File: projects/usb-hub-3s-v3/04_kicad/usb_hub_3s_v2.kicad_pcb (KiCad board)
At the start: 4 copper layers, 130 x 92 mm, 114 parts, among them J1 C98732, J2 C503996, J3 C503996, J4 C503996, J5 C5337088, Q1 C2760089, Q2 C404363, Q3 C404363, Q4 C404363, Q5 C404363, Q6 C2760089, Q7 C78284, SW1 C2939728, U10 C7519, U11 C13755, U12 C7519, U2 C13755, U3 C130056, U4 C130056, U5 C130056, U6 C473910, U7 C473910, U8 C7519, U9 C7519

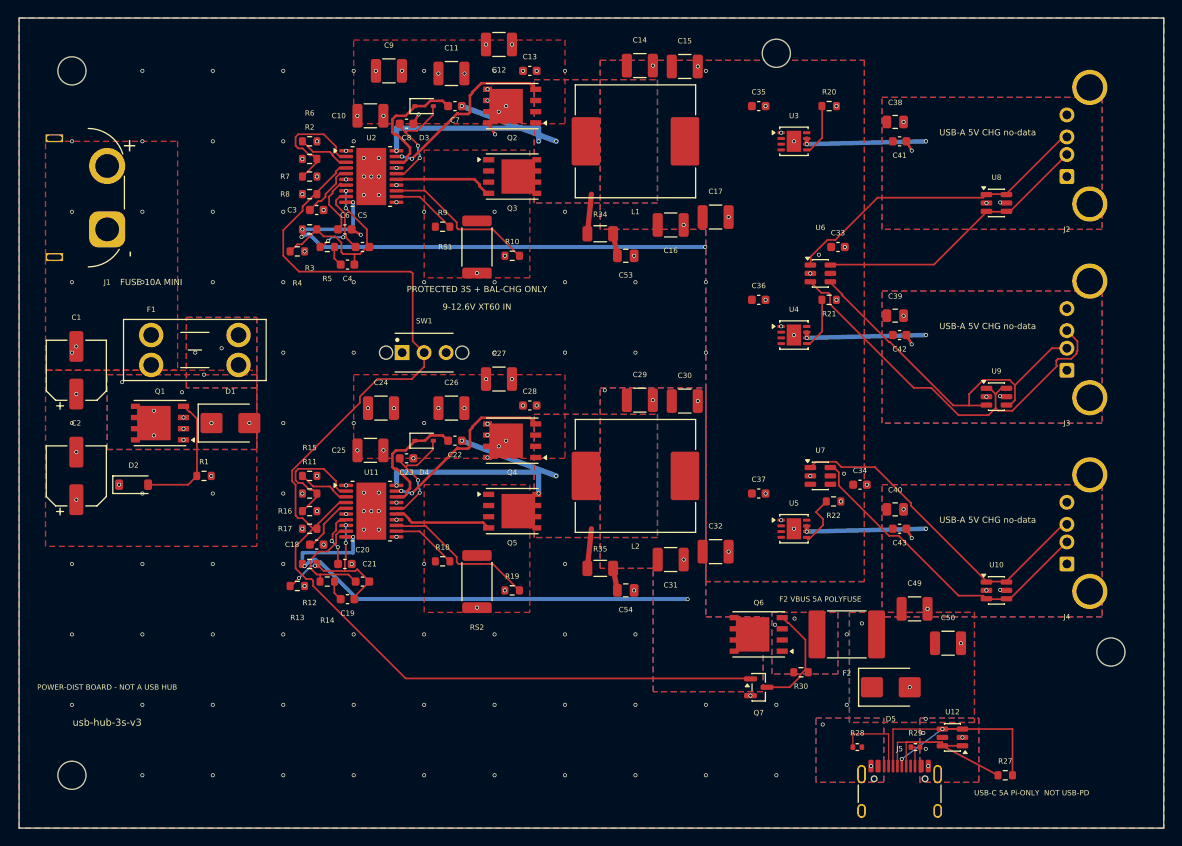
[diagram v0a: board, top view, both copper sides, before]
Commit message: usb-hub-3s-v3 v1.6: DRC 0/0/0 — the H3 screw-short is gone, and 11 CPL rows were off JLC's datum
v1.5 is DO-NOT-ORDER, and not for a reason any render could show. A new A-POS
gate measured every CPL row against JLC's convention — JLC positions a part
from the bounding box of its PAD CENTRES — and found the exporter had been
emitting fp.GetPosition(), the footprint ANCHOR. 11 of 108 rows were off-datum:
J1 4.6861mm, J2/J3/J4 3.7346mm, J5 1.4975mm, Q4/Q5/Q6 0.0625mm. Every external
connector, worst by nearly 5mm.

COPPER, all measured on FILLED zones before and after.

H3 was a short of the 6A rail to GND through a screw. MEASURED on sealed v1.5:
H3 (106,24) is a 1.600mm-radius NPTH whose F.Cu carries GND at 1.850mm AND 5VA
at 1.850mm, and whose B.Cu carries 5VA at 1.850 AND GND at 1.851. 0.250mm of
bare laminate and ~20um of mask, on both faces. EVERY M3 fastener bridges it —
not just a big washer, the smallest cap head (r 2.75) already does. v1.5's only
mitigation was a sentence in ORDER_README about nylon standoffs, which survives
exactly as long as the person who read it.

So v1.6 states a RULE instead of a note: within r <= 4.00mm of any mounting
hole, all outer copper is ONE net and that net is GND. Enforced three ways —
the 5VA pour is notched (5VA now stops at 4.500mm), the router's hole keepout
goes 3.0 -> 4.2mm so a signal wave cannot re-create it on a different net, and
the check is re-measured on the final filled board rather than assumed.

Also: H4's VBUSA3 4.152 -> 5.008mm (a DIN 9021 washer reached it); the In2 VIN
plane 1.850 -> 2.077mm on all four drills (0.250mm to a 12.6V plane, against a
+-0.13mm NPTH position tolerance, buried where no inspection will ever see it).
In1 GND is deliberately left at 1.850 — a grounded fastener touching GND is the
benign case and thinning the return plane costs more than it buys.

VBUS ampacity 0.5 -> 0.8mm. "Pour-fed" was true of the connector end and false
of the feed: each of VBUSA1/2/3 ran 13.554mm of 0.500mm B.Cu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
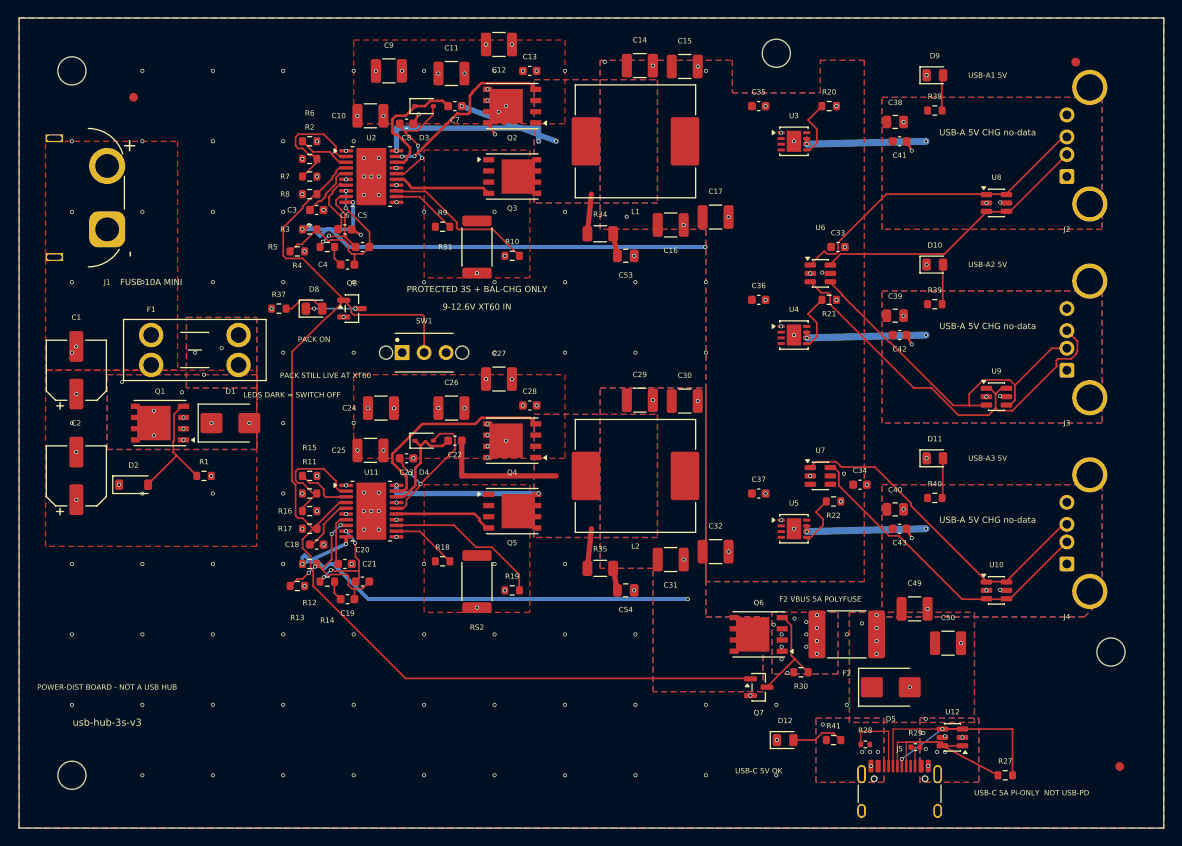
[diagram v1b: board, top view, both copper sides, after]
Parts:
- added D10: C2297, LED_SMD:LED_0805_2012Metric, F.Cu at (124.0, 48.0)
- added D11: C2297, LED_SMD:LED_0805_2012Metric, F.Cu at (124.0, 70.0)
- added D12: C2297, LED_SMD:LED_0805_2012Metric, F.Cu at (107.0, 102.0)
- added D8: C2296, LED_SMD:LED_0805_2012Metric, F.Cu at (53.5, 53.0)
- added D9: C2297, LED_SMD:LED_0805_2012Metric, F.Cu at (124.0, 26.5)
- added FID1: Fiducial_1mm_Mask2mm, Fiducial:Fiducial_1mm_Mask2mm, F.Cu at (33.0, 29.0)
- added FID2: Fiducial_1mm_Mask2mm, Fiducial:Fiducial_1mm_Mask2mm, F.Cu at (140.0, 25.0)
- added FID3: Fiducial_1mm_Mask2mm, Fiducial:Fiducial_1mm_Mask2mm, F.Cu at (145.0, 105.0)
- added Q8: C78284, Package_TO_SOT_SMD:SOT-23, F.Cu at (57.8, 53.0)
- added R37: 6.98kΩ, Resistor_SMD:R_0603_1608Metric, F.Cu at (49.5, 53.0)
- added R38: 6.98kΩ, Resistor_SMD:R_0603_1608Metric, F.Cu at (124.0, 30.5)
- added R39: 6.98kΩ, Resistor_SMD:R_0603_1608Metric, F.Cu at (124.0, 52.5)
- added R40: 6.98kΩ, Resistor_SMD:R_0603_1608Metric, F.Cu at (124.0, 74.5)
- added R41: 6.98kΩ, Resistor_SMD:R_0603_1608Metric, F.Cu at (112.5, 102.0)
- Q1, Q2, Q3, Q4, Q5, Q6: footprint Package_SO:PowerPAK_SO-8_Single -> usb_hub_3s:PowerPAK_SO-8_Single_Paste65
- moved R28 0.95 mm to (116.1, 102.5)
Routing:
- net LEDPKK: track 0.00 -> 6.17 mm, vias 0 -> 2
- net LEDVC: track 0.00 -> 6.13 mm
- net VCC_C: track 13.0 -> 18.3 mm
- net LEDPK: track 0.00 -> 4.99 mm
- net LEDVA3: track 0.00 -> 4.60 mm
- net LEDVA2: track 0.00 -> 4.60 mm
- net LEDVA1: track 0.00 -> 4.10 mm
- net HO_C: track 20.9 -> 24.2 mm, vias 2 -> 0
- net ENKILL: track 136.0 -> 133.5 mm
- net BOOT_C: track 14.4 -> 12.1 mm
- net 5VC: track 55.7 -> 53.6 mm, vias 4 -> 3
- net COMP_C: track 13.4 -> 11.4 mm, vias 0 -> 4
- net VIN: track 4.09 -> 2.83 mm, vias 33 -> 34
- net FB_C: track 19.0 -> 20.1 mm
- net ILIM2: track 5.98 -> 6.89 mm
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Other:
- board text added: "D10"
- board text added: "D11"
- board text added: "D12"
- board text added: "D8"
- board text added: "D9"
- board text added: "FID1"
- board text added: "FID2"
- board text added: "FID3"
- board text added: "LEDS DARK = SWITCH OFF"
- board text added: "PACK ON"
- board text added: "PACK STILL LIVE AT XT60"
- board text added: "Q8"
- board text added: "R37"
- board text added: "R38"
- board text added: "R39"
- board text added: "R40"
- board text added: "R41"
- board text added: "USB-A1 5V"
- board text added: "USB-A2 5V"
- board text added: "USB-A3 5V"
- board text added: "USB-C 5V OK"

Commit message: usb-hub-3s-v3 v1.6: the load is a Pi 4, not a Pi 5 — the margin was never 15mV
Every power document on this board rested on one sentence, recorded at
commission as a "user + web-confirmed finding": that the Pi can be told to skip
PD negotiation and assume a 5A supply via `PSU_MAX_CURRENT=5000`.

THAT IS A RASPBERRY PI 5 BOOTLOADER-EEPROM FEATURE. The user has confirmed the
load is a Pi 4, which has no such setting and no equivalent.

The conclusion it justified — no PD source controller — survives. The reasoning
does not, and the difference is not cosmetic. A Pi 5 IS a PD sink; the old story
was "talk it out of negotiating", a deliberate departure from the normal
interface. A Pi 4 does not negotiate PD for its power input AT ALL: its USB-C
input is a plain 5V sink with CC pull-downs, officially 5V/3A (15W). There is no
profile to request and no override to set. A plain regulated rail is not a
workaround for a Pi 4 — it is the only interface it has.

An ADR whose stated reason is false is worse than no ADR, because it looks
decided. This fleet proved that twice today (cooksense's LMV393 "rail-to-rail"
claim, and this). So the digit is not swapped: ADR-0001 is marked
`superseded-by: 0004` (REASONING ONLY, its decision stands), ADR-0004 makes the
correct argument, and BRIEF.md keeps the old paragraph STRUCK rather than
deleted so the record of what was believed survives. T1 is rewritten (the
tension was never real), T3 is VOID (nothing for the user to forget), T4 is
added. `PSU_MAX_CURRENT` is purged from every live document — tsx header,
ARCHITECTURE, DETAIL_DESIGN, power_tree — and left only in the historical
reviews and the struck BRIEF text.

THE MARGIN IMPROVES 16.5x. Same hardware, same 97 mOhm budget, same 1.2
derating, same 5.227V worst-case rail, same 4.63V threshold. Only the load
changed, because we now know what it is:

    Pi 5 premise @ 5A: 582.0 mV drop -> 4.645 V ->  +15.0 mV slack
    Pi 4 actual  @ 3A: 349.2 mV drop -> 4.878 V -> +247.8 mV slack

E-MA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
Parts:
- added R42: 160kΩ, Resistor_SMD:R_0402_1005Metric, F.Cu at (50.5, 87.0)
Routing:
- net 5VC: track 53.6 -> 60.8 mm, vias 3 -> 4
- net COMP_A: track 11.3 -> 18.4 mm
- net 5VA: track 57.3 -> 53.3 mm, vias 8 -> 6
- net FB_C: track 20.1 -> 22.8 mm
- net DM_A2: track 41.8 -> 44.2 mm
- net DP_A2: track 48.4 -> 46.6 mm
- net SS_A: track 7.24 -> 6.02 mm
- net FB_A: track 20.9 -> 19.7 mm
- net GND: track 6.08 -> 4.88 mm, vias 181 -> 178
- net ILIM3: track 6.25 -> 5.37 mm
- net SS_C: track 6.02 -> 6.85 mm
- net ILIM2: track 6.89 -> 6.06 mm
- net ILIM1: track 6.89 -> 6.06 mm
- net QG: track 12.1 -> 12.9 mm
- net CSGF_C: track 18.1 -> 17.5 mm
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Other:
- board text added: "R42"

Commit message: usb-hub-3s-v3 v1.6: export on-datum, twin 119/119, and the GND return that was missing
EXPORT VERIFIED, and the two things that killed v1.5 are gone:

  A-ROT OK: all 119 CPL rotations sourced from measured per-LCSC rows.
  A-POS datum: 119 rows graded, WORST 0.00050mm (Q6) against a 0.05mm tolerance.
  v1.5 had 11 of 108 rows off JLC's pad-centre datum — J1 4.6861, J2-J4 3.7346,
  J5 1.4975, Q4-Q6 0.0625mm — because the exporter emitted the footprint ANCHOR.
  J1's CPL row now reads (27.0, -40.4), the pad-array centre, not (30.0, -44.0).

  ALL FIVE INDICATOR LEDS EXPORT AT ROTATION 0.0. That was the one thing worth
  re-checking by hand, because the confident answer is 180 and 180 ships them dark.

THE TWIN AGREES WITH ME, BY A METHOD I DID NOT WRITE. jlc_twin's marking channel
independently reports "the pad-number fit says offset 180, but the MARKING channel
disagrees by 180deg: our polarity marking sits at pad 1 (margin 0.69mm) while
JLC's sits at pad 2 (margin 0.23mm) — the two libraries NUMBER this part's
terminals oppositely, so the pad fit is 180deg wrong PHYSICALLY". Three
implementations now agree on 0: jlc_rotation_measure's polarity channel, a hand
cathode-to-cathode read, and this. Canon M1 satisfied by accident of good design.

Its ROT-DB-SUGGEST still proposes "add C2296,180" from the pad fit alone,
contradicting its own POLARITY-FIT finding two lines above. Adjudicated REJECTED
with the reason, not waived, and reported upstream. It cannot reach the export,
which resolves from the measured row.

bodies mounted 119/119, generated missing_models.txt, twin exits 0. Four
adjudications, each with a measurement rather than a rationale:
  - C2296/C2297 POLARITY-FIT/CHECK/ROT-DB-SUGGEST -> offset 0, with both
    numbering-free channels written out;
  - F1 PAD-MULTIPLICITY (our land models each fuse CLIP as a plated-hole PAIR,
    9.92mm real Keystone pitch vs JLC's 3.40mm 2-pad model) and MODEL-REG (newly
    blocking after Stage 0; most of the 5.0mm offset 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
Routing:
- net 5VC: vias 4 -> 3

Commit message: usb-hub-3s-v3 v1.6 STAGED, NOT SEALED: M-REPRO fails on generator nondeterminism
Every board gate is green. The release is staged, complete, and NOT ORDERABLE,
because the one thing canon M3 promises — the same source yields the same board —
is not currently true of this pipeline.

THREE from-source regenerations of IDENTICAL source: 292 / 294 / 293 vias.
Three distinct numbers is the answer to the question. Had the third returned 294
this would have been deterministic island rescue responding to a one-time input
delta, worth a line and nothing more. It did not.

Everything else is identical across all three runs — footprints 129, tracks 908,
track length 1070.469mm, zones 51, pads 457, nets 74. The whole delta is
island-rescue vias on the 5VA/5VC pours, plus one via that MOVED BY 0.010mm
((110.830,46.900) -> (110.830,46.910)), which is the tell: that is a tessellation
boundary, not a routing decision.

ROOT CAUSE MEASURED, and it is not in this board. generate_board_generic.py mints
fresh random UUIDs every run — 129/129 footprint UUIDs differ between two runs of
the same source. KiCad serialises footprints in UUID order, so the reference order
differs at index 0 and in 129/129 positions. The zone filler then walks zones in a
different order, Clipper tessellates pour boundaries differently, and
island_rescue keys off exactly those islands. Same mechanism cooksense diagnosed.

DELIBERATELY NOT FIXED HERE. Deterministic UUIDs in generate_board_generic.py is
a fleet task; nothing in 03_src/ or 03_tscircuit/ can make this pipeline
reproducible while the generator randomises identity every run. Attempting it
from a board revision would be the wrong place and would couple a fleet change to
one board's seal.

The board is not wrong: all three runs are DRC 0/0/0 and the extra vias are
additive same-net island bonds — island_rescue doing its job. The release seals
when deterministic UUIDs land and one clean regeneration matches the staged copy.

EXPORT VERIFIED (the three t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
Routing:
- net 5VC: vias 3 -> 4
